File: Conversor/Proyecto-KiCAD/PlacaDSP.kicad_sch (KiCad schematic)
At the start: 0 parts

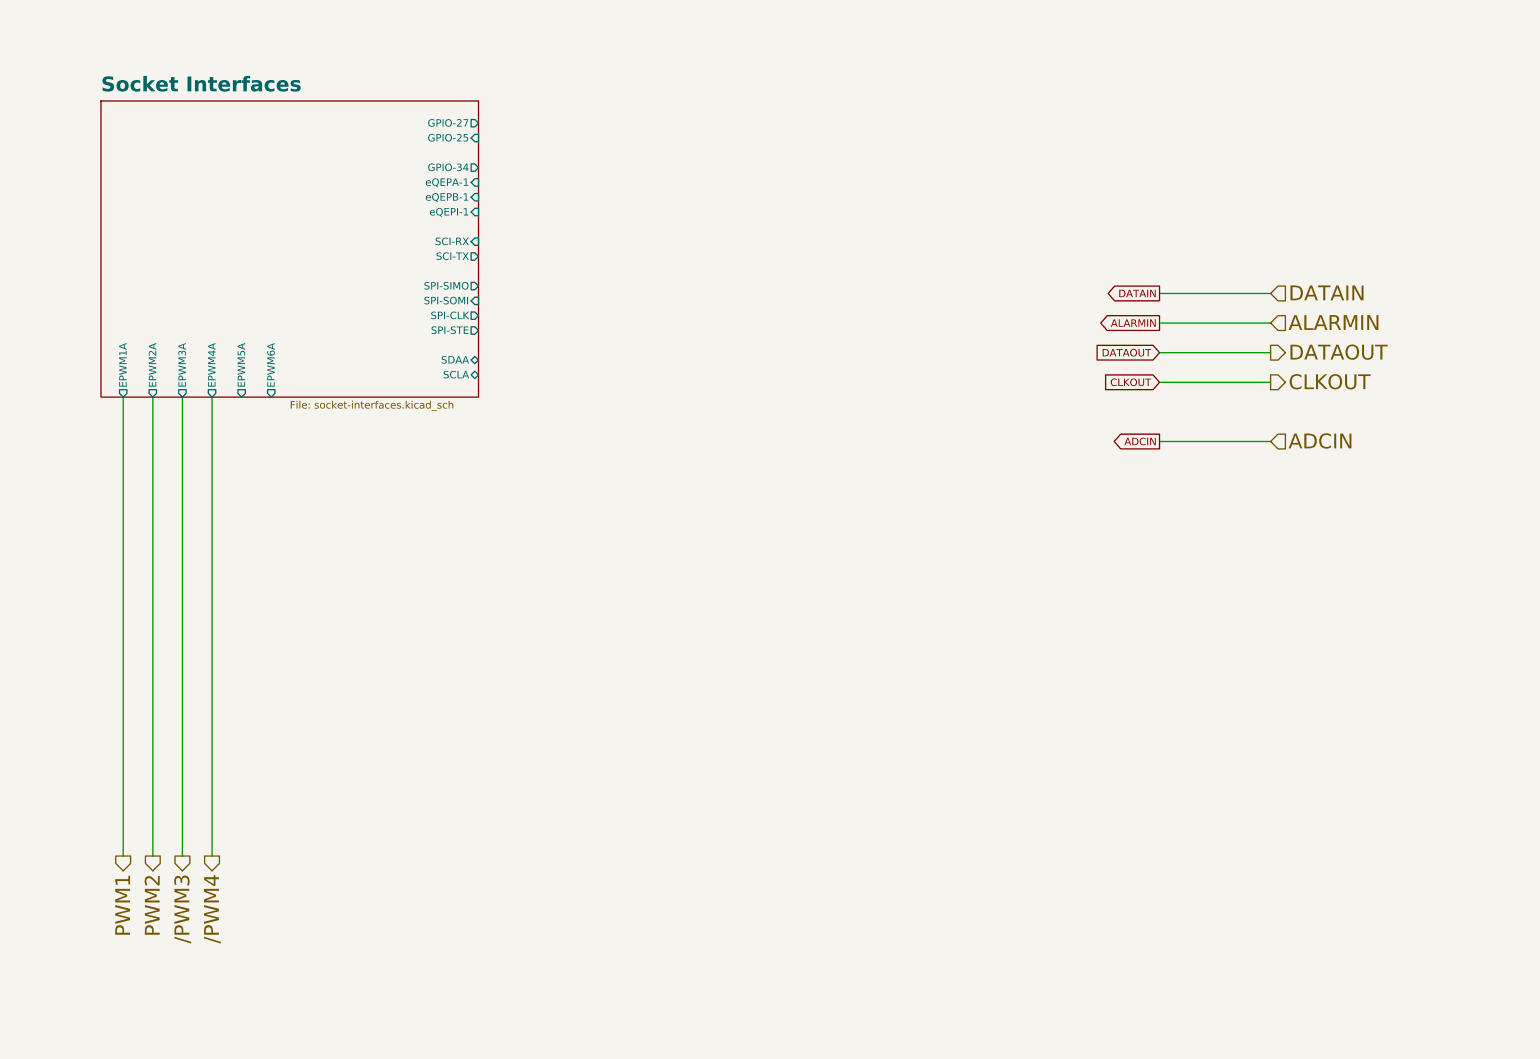
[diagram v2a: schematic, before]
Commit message: Continuar el paso de la placa adaptadora al proyecto
- El bloque de encoder y DAC se eliminan, no son necesarios
- Hay que agregar un selector entre 5V externo y por USB para el DSP, y ver como compatibilizarlo con la alimentación general
- Para el regulador de 3.3V se usa el mismo integrado que en la placa adaptadora (TI LP2985-3.3)
- Los optos son los ACPL-P480 en vez de los P343
Por hacer:
  - Terminar la placa adaptadora (USB-UART, Power Supply e I2C)
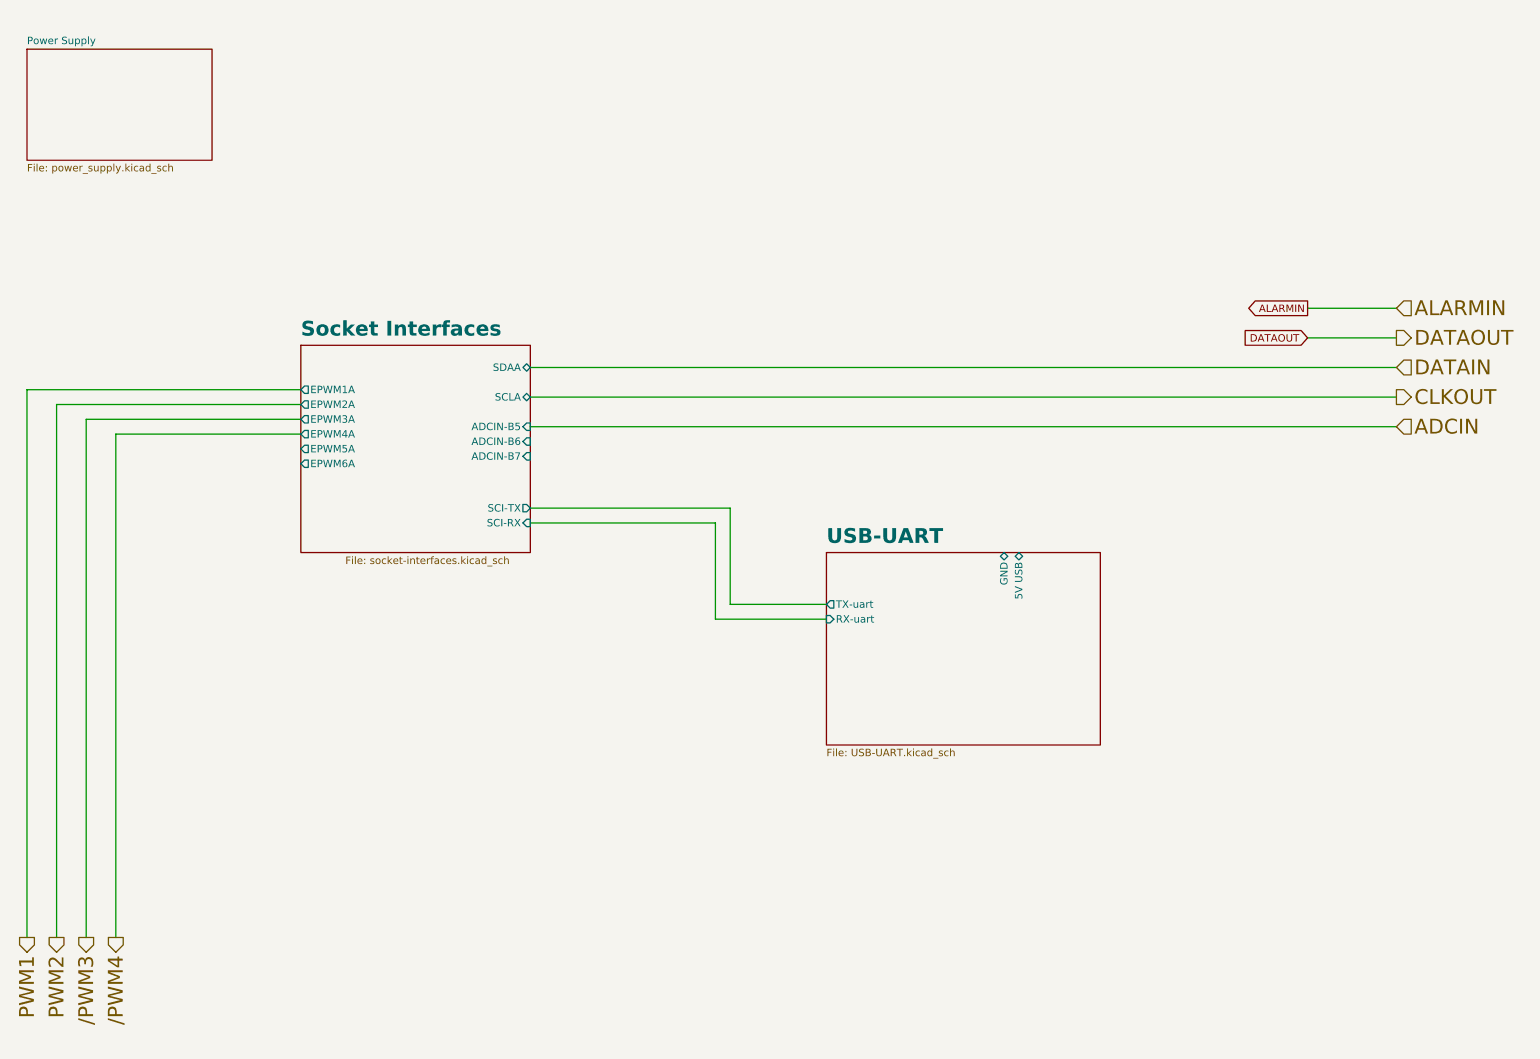
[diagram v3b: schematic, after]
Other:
- added sheet Power Supply (power_supply.kicad_sch)
- added sheet USB-UART (USB-UART.kicad_sch)
- sheet Socket Interfaces ports: added ADCIN-B5, ADCIN-B6, ADCIN-B7; removed GPIO-25, GPIO-27, GPIO-34, SPI-CLK, SPI-SIMO, SPI-SOMI, SPI-STE, eQEPA-1, eQEPB-1, eQEPI-1

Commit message: Terminar (casi) el traspaso de la placa adaptadora al proyecto
- Queda el selector entre 5V USB y 5V extern, pero todo esta en la hoja
de alimetación general, no dentro de la hoja del DSP
- Cambiar un poco los headers para poder testear (separado en Headers
5V, PWM, ADC, UART, I2C y GPIO)
- Agregar la hoja de datos del LP2985-3.3 (regulador de +3V3)
Por hacer:
  - Ver el tema de la asilacion de las lineas de datos I2C del LM5056,
porque tiene que unirse a una sola linea de datos bidireccional a la
salida del aislador (estan separadas para facilitar la aislación)
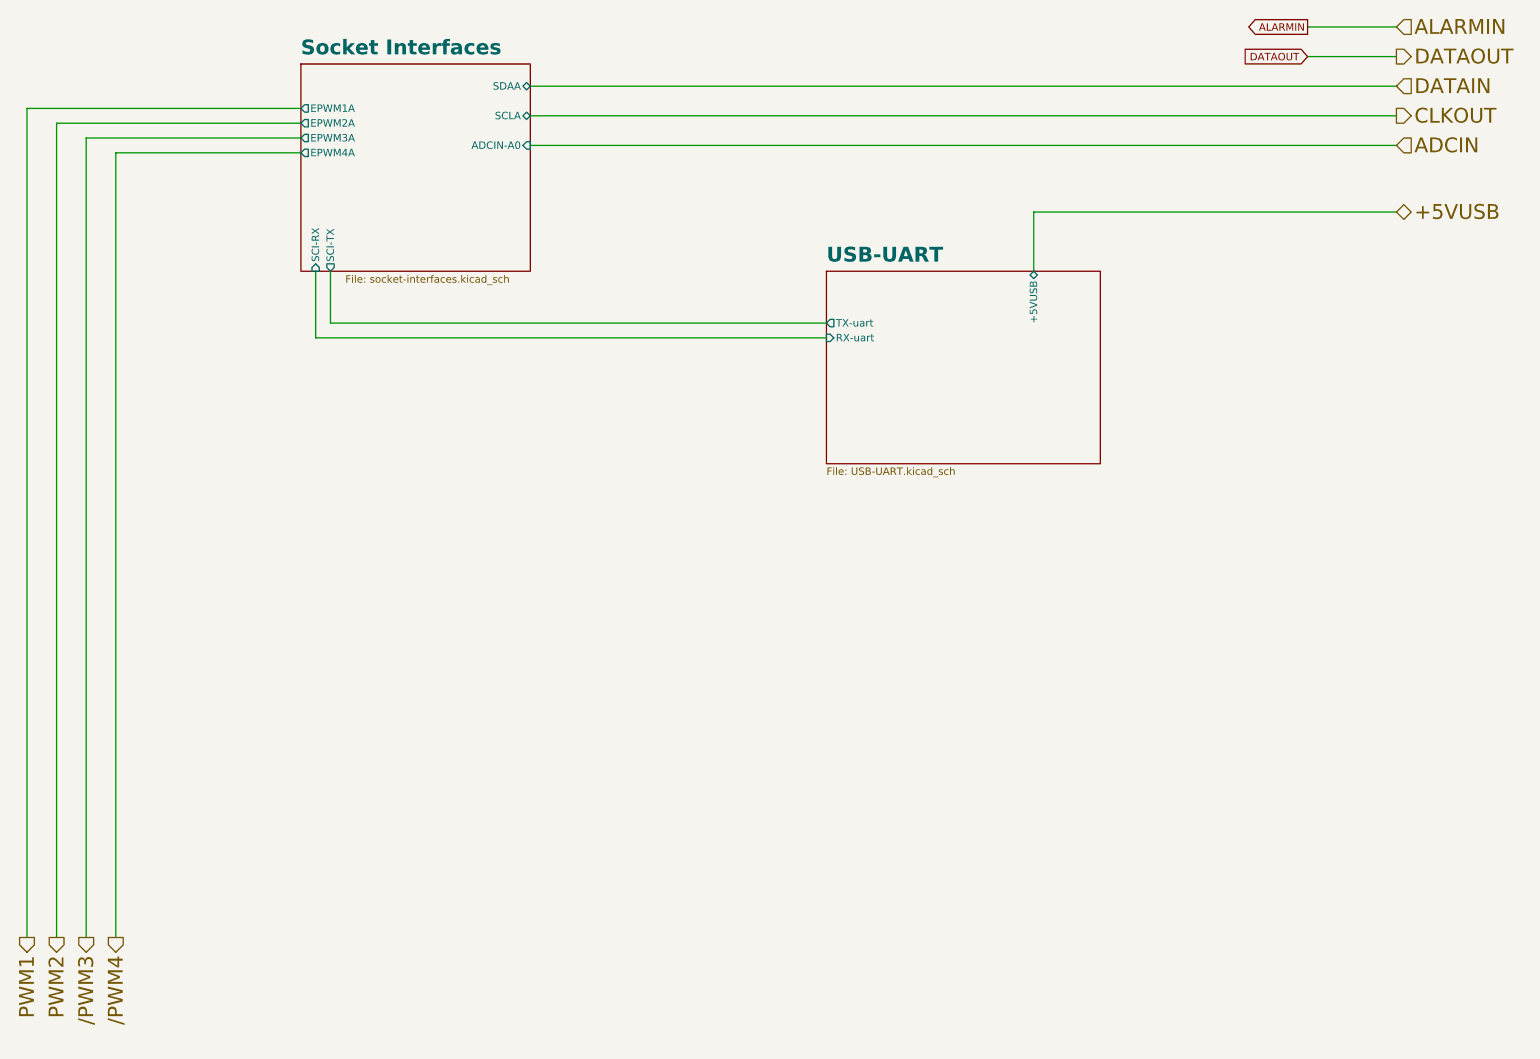
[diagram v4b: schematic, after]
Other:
- removed sheet Power Supply
- sheet Socket Interfaces ports: added ADCIN-A0; removed ADCIN-B5, ADCIN-B6, ADCIN-B7, EPWM5A, EPWM6A
- sheet USB-UART ports: added +5VUSB; removed 5V USB, GND

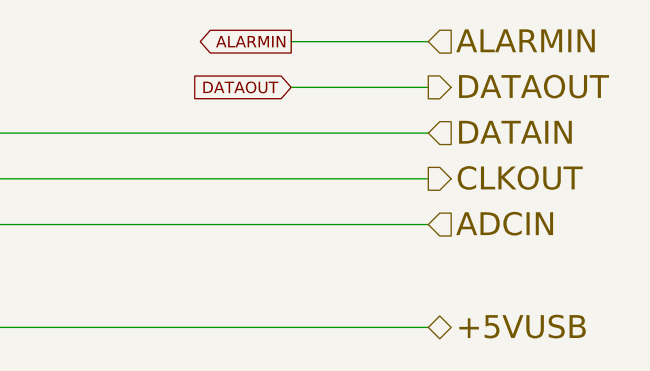
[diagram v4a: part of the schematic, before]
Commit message: Unir las lineas de SDAI y SDAO a la salida del ISO7242C
- Espejar el esquemático en la hoja de sensores, para que sea consistente la separación de Digital/Potencia
Por hacer:

  - Verificar si es correcta la forma de conectar las lineas de datos a la salida del aislador
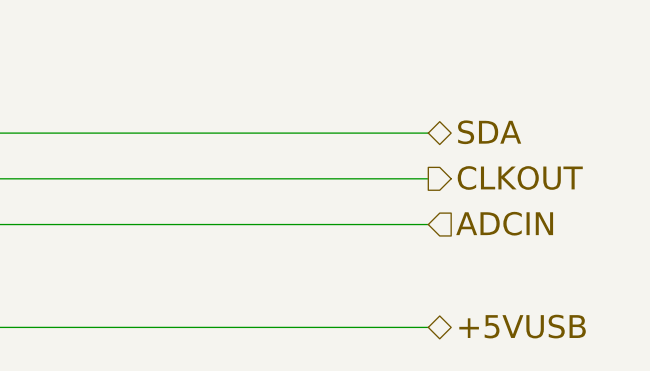
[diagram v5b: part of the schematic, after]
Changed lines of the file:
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@@
-    (stroke (width 0) (type default) (color 0 0 0 0))
-  )
-  (wire (pts (xy 245.11 22.86) (xy 260.35 22.86))
     (stroke (width 0) (type default) (color 0 0 0 0))
   )
@@
     (stroke (width 0) (type default) (color 0 0 0 0))
   )
-  (wire (pts (xy 245.11 17.78) (xy 260.35 17.78))
-    (stroke (width 0) (type default) (color 0 0 0 0))
-  )
-  (global_label "ALARMIN" (shape output) (at 245.11 17.78 180) (fields_autoplaced)
-    (effects (font (size 1.27 1.27)) (justify right))
-    (property "Intersheet References" "${INTERSHEET_REFS}" (id 0) (at 234.835 17.7006 0)
-      (effects (font (size 1.27 1.27)) (justify right) hide)
-    )
-  )
-  (global_label "DATAOUT" (shape input) (at 245.11 22.86 180) (fields_autoplaced)
-    (effects (font (size 1.27 1.27)) (justify right))
-    (property "Intersheet References" "${INTERSHEET_REFS}" (id 0) (at 234.6536 22.7806 0)
-      (effects (font (size 1.27 1.27)) (justify right) hide)
-    )
-  )
-  (hierarchical_label "DATAOUT" (shape output) (at 260.35 22.86 0)
-    (effects (font (size 2.54 2.54)) (justify left))
-  )
-  (hierarchical_label "ALARMIN" (shape input) (at 260.35 17.78 0)
+  (hierarchical_label "SDA" (shape bidirectional) (at 260.35 27.94 0)
     (effects (font (size 2.54 2.54)) (justify left))
   )
@@
     (effects (font (size 2.54 2.54)) (justify right))
   )
-  (hierarchical_label "DATAIN" (shape input) (at 260.35 27.94 0)
-    (effects (font (size 2.54 2.54)) (justify left))
-  )
   (hierarchical_label "{slash}PWM3" (shape output) (at 35.56 173.99 270)
